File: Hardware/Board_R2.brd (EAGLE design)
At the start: 100.3 x 45.7 mm, 53 parts, among them U1 EDISON_CONNECTOR_FULLMOUNTING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, U2 LAN9512-JZX, U3 MAX4995AAUT+, U4 EDISON_CONNECTOR_FULLHEADER, X1 J1011F01P

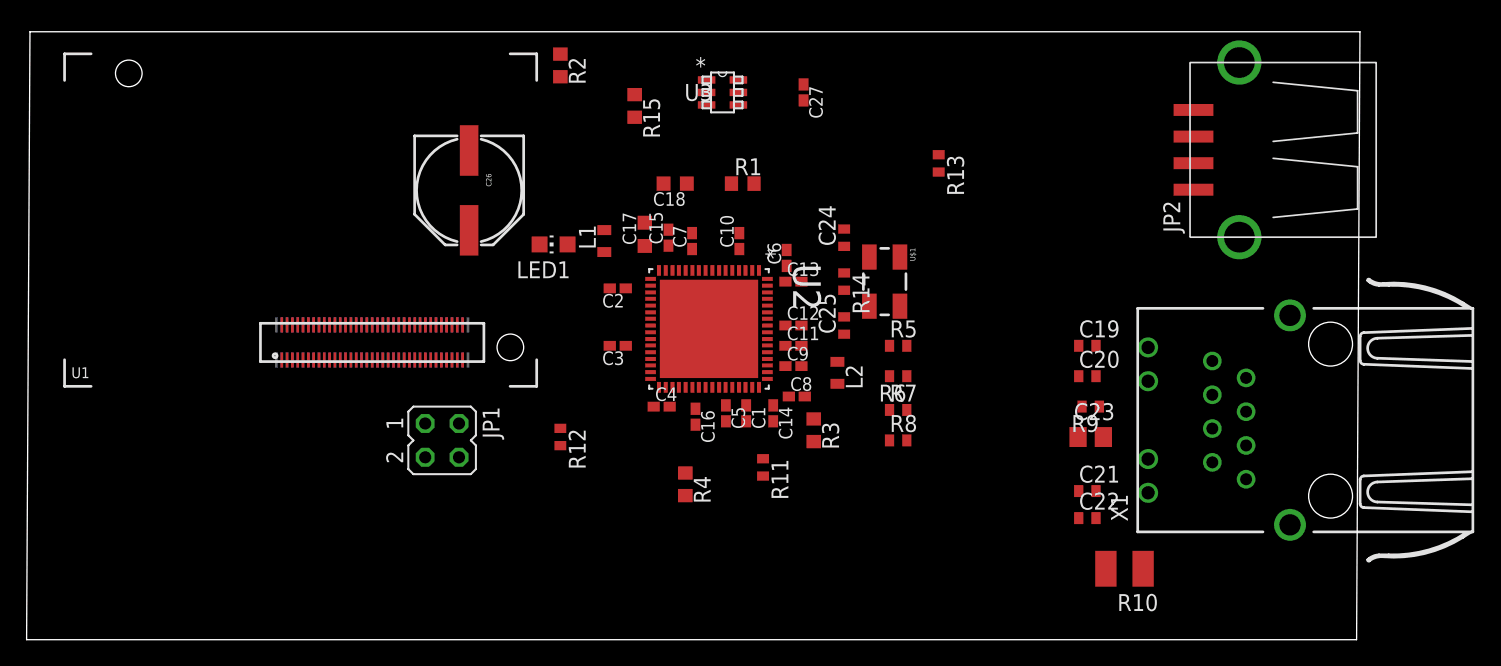
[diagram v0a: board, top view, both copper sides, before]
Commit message: Added intitial 4 layer board layout and made very minor changes to Schematic and BOM.
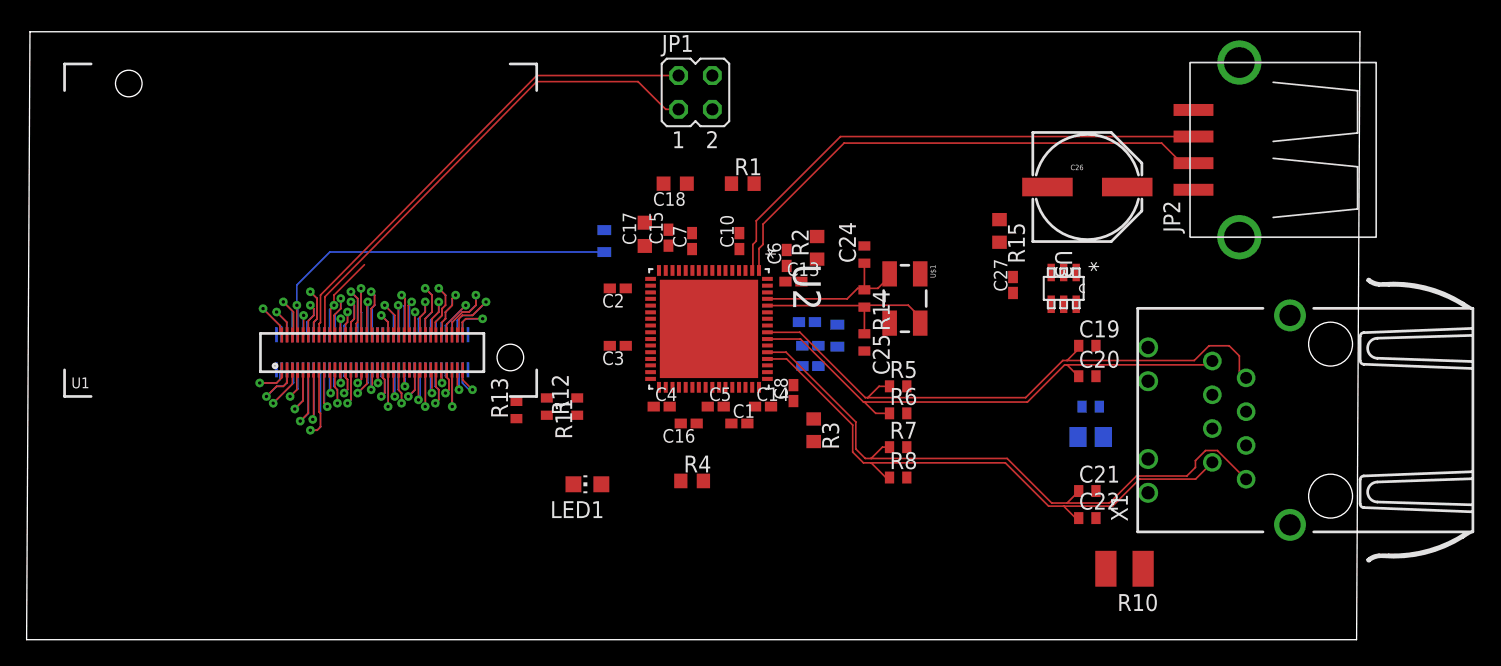
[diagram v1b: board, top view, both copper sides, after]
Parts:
- moved C26 46.5 mm to (80.0, 34.3), turned to 0 degrees
- moved R13 36.8 mm to (37.1, 17.5), turned to 90 degrees
- moved JP1 32.4 mm to (50.5, 41.4), turned to 0 degrees
- moved U3 29.6 mm to (78.2, 26.7), turned to 270 degrees
- moved R15 29.0 mm to (73.4, 31.0)
- moved R2 23.7 mm to (59.7, 29.7), turned to 90 degrees
- moved C27 21.4 mm to (74.4, 26.9), turned to 90 degrees
- moved LED1 18.2 mm to (42.4, 11.9)
- moved R11 16.9 mm to (39.4, 17.8)
- moved R5 3.05 mm to (65.8, 19.3)
- moved L2 2.79 mm to (61.2, 23.1), flipped to the bottom
- moved R6 2.79 mm to (65.8, 17.3), turned to 0 degrees
- moved R7 2.79 mm to (65.8, 14.7)
- moved R8 2.79 mm to (65.8, 12.4)
- moved R12 2.62 mm to (41.7, 17.8), turned to 90 degrees
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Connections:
- net N$11 renamed RX_P
- net N$12 renamed RX_N
- net N$13 renamed TX_N
- net N$14 renamed TX_P
- net N$24 renamed DSUSB_N
- net N$5 renamed DSUSB_P
- net +3V3: now also LED1.A; no longer R13.1
- net N$19: now also R13.1; no longer U2.20
- net N$20: now also U2.20; no longer LED1.A
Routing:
- net RX_P: track 0.00 -> 47.7 mm
- net TX_N: track 0.00 -> 44.8 mm
- net RX_N: track 0.00 -> 43.9 mm
- net GND: track 0.00 -> 43.6 mm, vias 0 -> 6
- net TX_P: track 0.00 -> 40.2 mm
- net DSUSB_P: track 0.00 -> 39.4 mm
- net DSUSB_N: track 0.00 -> 39.3 mm
- net USBUP2: track 0.00 -> 37.1 mm
- net USBUP: track 0.00 -> 36.9 mm
- net +3V3: track 0.00 -> 33.1 mm, vias 0 -> 2
- net N$22: track 0.00 -> 14.4 mm
- net N$21: track 0.00 -> 12.2 mm
- net USB_VBUS: track 0.00 -> 8.95 mm, vias 0 -> 1
- net P66: track 0.00 -> 8.06 mm, vias 0 -> 1
- net P60: track 0.00 -> 8.04 mm, vias 0 -> 1
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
